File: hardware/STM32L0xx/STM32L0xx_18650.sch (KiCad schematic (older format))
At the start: 50 parts, among them J1 Debug, J2 Battery, J3 GPIO, J4 USB_B_Micro, J5 Power, J6 LEDs, J7 GPIO, Q1 BSS806N, Q2 BSS806N, Q3 BSS806N, Q4 BSS806N, SW1 Mode, SW2 Power, U1 STM32L072CBTx, U2 AP2210N-3.3TRG1, U3 MCP73831T-2ACI/OT, Y1 32.768kHz

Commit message: Add a full 10-pin JTAG connector.
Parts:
- added J8, J9: Conn_01x01, Connector_PinHeader_2.54mm:PinHeader_1x01_P2.54mm_Vertical, symbol Connector_Generic:Conn_01x01
- J1: value Debug -> SW Debug; footprint Connector_PinHeader_1.27mm:PinHeader_1x03_P1.27mm_Vertical -> Connector_PinHeader_1.27mm:PinHeader_2x05_P1.27mm_Vertical; symbol Connector_Generic:Conn_01x03 -> Connector:Conn_ARM_JTAG_SWD_10
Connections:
- wire segments 202 -> 209
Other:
- note added: "JTAG / SWD"
- moved on the sheet: U2
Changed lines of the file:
@@
-$EndComp
-$Comp
-L power:+3V3 #PWR0102
-U 1 1 5BD53A46
-P 5050 6900
-F 0 "#PWR0102" H 5050 6750 50  0001 C CNN
-F 1 "+3V3" H 5065 7073 50  0000 C CNN
-F 2 "" H 5050 6900 50  0001 C CNN
-F 3 "" H 5050 6900 50  0001 C CNN
-	1    5050 6900
-	1    0    0    -1
 $EndComp
 $Comp
@@
 Connection ~ 2700 7400
 NoConn ~ 3050 7100
-$Comp
-L power:GND #PWR0108
-U 1 1 5BD85B6B
-P 4500 7450
-F 0 "#PWR0108" H 4500 7200 50  0001 C CNN
-F 1 "GND" H 4505 7277 50  0000 C CNN
-F 2 "" H 4500 7450 50  0001 C CNN
-F 3 "" H 4500 7450 50  0001 C CNN
-	1    4500 7450
-	1    0    0    -1
-$EndComp
 Text Label 1700 1450 0    50   ~ 0
 VIN
 Wire Wire Line
 	1500 1450 1700 1450
-Text Label 4100 7000 2    50   ~ 0
-VIN
 $Comp
 L STM32L0xx_18650-rescue:MCP73831T-2ACI_OT-LEDRibbonController-rescue-LitFist18650-rescue U?
@@
 Text Notes 2450 6450 0    50   ~ 0
 USB Connector
-Wire Wire Line
-	5050 6900 5050 7000
-Wire Wire Line
-	5050 7000 4950 7000
-Text Notes 3950 6650 0    50   ~ 0
-3.3v Power
 $Comp
 L Transistor_FET:MMBF170 Q?
@@
 Wire Wire Line
 	10100 5400 10400 5400
-$Comp
-L Jeremy:AP2210-3.3TRG1 U2
-U 1 1 5CD3E552
-P 4250 7050
-F 0 "U2" H 4350 6750 50  0000 C CNN
-F 1 "AP2210N-3.3TRG1" H 4525 7234 50  0000 C CNN
-F 2 "Package_TO_SOT_SMD:SOT-23" H 4200 7450 50  0001 C CNN
-F 3 "" H 4200 7450 50  0001 C CNN
-F 4 "AP2210N-3.3TRG1" H 4250 7050 50  0001 C CNN "MPN"
-	1    4250 7050
-	1    0    0    -1
-$EndComp
-Wire Notes Line
-	3950 6650 5200 6650
-Wire Notes Line
-	5200 6650 5200 7700
-Wire Notes Line
-	3950 7700 5200 7700
-Wire Notes Line
-	3950 6650 3950 7700
 Wire Wire Line
 	4450 2800 4300 2800
@@
 Wire Notes Line
 	2450 6450 3700 6450
-Text Label 1850 6100 0    50   ~ 0
-SWDIO
-Text Label 1850 6000 0    50   ~ 0
-SWCLK
-Text Label 1850 5900 0    50   ~ 0
-RESET
 $Comp
 L Device:R R?
@@
 	0    1    1    0
 $EndComp
-$Comp
-L Connector_Generic:Conn_01x03 J1
+Text Label 4800 6800 0    50   ~ 0
+SWDIO
+Text Label 4800 6700 0    50   ~ 0
+SWCLK
+Text Label 4800 6500 0    50   ~ 0
+RESET
+$Comp
+L power:+3.3V #PWR0104
+U 1 1 5D7E89AF
+P 4300 6200
+F 0 "#PWR0104" H 4300 6050 50  0001 C CNN
+F 1 "+3.3V" H 4315 6373 50  0000 C CNN
+F 2 "" H 4300 6200 50  0001 C CNN
+F 3 "" H 4300 6200 50  0001 C CNN
+	1    4300 6200
+	1    0    0    -1
+$EndComp
+$Comp
+L power:GND #PWR0105
+U 1 1 5D7E99F4
+P 4250 7450
+F 0 "#PWR0105" H 4250 7200 50  0001 C CNN
+F 1 "GND" H 4255 7277 50  0000 C CNN
+F 2 "" H 4250 7450 50  0001 C CNN
+F 3 "" H 4250 7450 50  0001 C CNN
+	1    4250 7450
+	1    0    0    -1
+$EndComp
+Wire Wire Line
+	4200 7400 4200 7450
+Wire Wire Line
+	4200 7450 4250 7450
+Wire Wire Line
+	4250 7450 4300 7450
+Wire Wire Line
+	4300 7450 4300 7400
+Connection ~ 4250 7450
+Wire Wire Line
+	4800 6900 4800 7000
+Wire Wire Line
+	4800 7450 4300 7450
+Connection ~ 4800 7000
+Wire Wire Line
+	4800 7000 4800 7450
+Connection ~ 4300 7450
+Wire Notes Line
+	3850 5950 3850 7700
+Wire Notes Line
+	5100 7700 5100 5950
+Wire Notes Line
+	3850 7700 5100 7700
+Wire Notes Line
+	3850 5950 5100 5950
+Wire Notes Line
+	5200 6650 5200 7700
+Wire Notes Line
+	5200 7700 6450 7700
+Wire Notes Line
+	6450 6650 6450 7700
+Wire Notes Line
+	5200 6650 6450 6650
+$Comp
+L Jeremy:AP2210-3.3TRG1 U2
+U 1 1 5CD3E552
+P 5500 7050
+F 0 "U2" H 5600 6750 50  0000 C CNN
+F 1 "AP2210N-3.3TRG1" H 5775 7234 50  0000 C CNN
+F 2 "Package_TO_SOT_SMD:SOT-23" H 5450 7450 50  0001 C CNN
+F 3 "" H 5450 7450 50  0001 C CNN
+F 4 "AP2210N-3.3TRG1" H 5500 7050 50  0001 C CNN "MPN"
+	1    5500 7050
+	1    0    0    -1
+$EndComp
+Text Notes 5200 6650 0    50   ~ 0
+3.3v Power
+Wire Wire Line
+	6300 7000 6200 7000
+Wire Wire Line
+	6300 6900 6300 7000
+Text Label 5350 7000 2    50   ~ 0
+VIN
+$Comp
+L power:GND #PWR0108
+U 1 1 5BD85B6B
+P 5750 7450
+F 0 "#PWR0108" H 5750 7200 50  0001 C CNN
+F 1 "GND" H 5755 7277 50  0000 C CNN
+F 2 "" H 5750 7450 50  0001 C CNN
+F 3 "" H 5750 7450 50  0001 C CNN
+	1    5750 7450
+	1    0    0    -1
+$EndComp
+$Comp
+L power:+3V3 #PWR0102
+U 1 1 5BD53A46
+P 6300 6900
+F 0 "#PWR0102" H 6300 6750 50  0001 C CNN
+F 1 "+3V3" H 6315 7073 50  0000 C CNN
+F 2 "" H 6300 6900 50  0001 C CNN
+F 3 "" H 6300 6900 50  0001 C CNN
+	1    6300 6900
+	1    0    0    -1
+$EndComp
+$Comp
+L Connector:Conn_ARM_JTAG_SWD_10 J1
 U 1 1 5D4460E4
-P 1650 6000
-F 0 "J1" H 1800 6000 50  0000 C CNN
-F 1 "Debug" H 1850 5900 50  0000 C CNN
-F 2 "Connector_PinHeader_1.27mm:PinHeader_1x03_P1.27mm_Vertical" H 1650 6000 50  0001 C CNN
-F 3 "~" H 1650 6000 50  0001 C CNN
-	1    1650 6000
-	-1   0    0    1
+P 4300 6800
+F 0 "J1" H 3950 6200 50  0000 C CNN
+F 1 "SW Debug" H 4550 6250 50  0000 C CNN
+F 2 "Connector_PinHeader_1.27mm:PinHeader_2x05_P1.27mm_Vertical" H 4300 6800 50  0001 C CNN
+F 3 "~" H 4300 6800 50  0001 C CNN
+	1    4300 6800
+	1    0    0    -1
+$EndComp
+Text Notes 3850 5950 0    50   ~ 0
+JTAG / SWD
+Connection ~ 800  6950
+Connection ~ 1200 6950
+$Comp
+L Connector_Generic:Conn_01x01 J8
+U 1 1 5D90FB9A
+P 800 7150
+F 0 "J8" V 900 7100 50  0000 L CNN
+F 1 "Conn_01x01" V 900 7050 50  0001 L CNN
+F 2 "Connector_PinHeader_2.54mm:PinHeader_1x01_P2.54mm_Vertical" H 800 7150 50  0001 C CNN
+F 3 "~" H 800 7150 50  0001 C CNN
+	1    800  7150
+	0    1    1    0
+$EndComp
+$Comp
+L Connector_Generic:Conn_01x01 J9
+U 1 1 5D9108FC
+P 1200 7150
+F 0 "J9" V 1300 7100 50  0000 L CNN
+F 1 "Conn_01x01" V 1300 7050 50  0001 L CNN
+F 2 "Connector_PinHeader_2.54mm:PinHeader_1x01_P2.54mm_Vertical" H 1200 7150 50  0001 C CNN
+F 3 "~" H 1200 7150 50  0001 C CNN
+	1    1200 7150
+	0    1    1    0
 $EndComp
 $EndSCHEMATC

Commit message: Change to 32 pin package.
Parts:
- removed C6: 100nf, Capacitor_SMD:C_0603_1608Metric, symbol Device:C_Small
- D1, D2: footprint Diode_SMD:D_SOD-323 -> Diode_SMD:D_SOD-323_HandSoldering
- U1: value STM32L072CBTx -> STM32L072KZTx; footprint Package_QFP:LQFP-48_7x7mm_P0.5mm -> Package_QFP:LQFP-32_7x7mm_P0.8mm; symbol MCU_ST_STM32L0:STM32L072CBTx -> MCU_ST_STM32L0:STM32L072KZTx; MPN STM32L072CBT6 -> STM32L072KZT6; Package 48-LQFP -> 32-LQFP
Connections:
- net +3V3: now also U1.17 (VDD); no longer U1.24 (VDD), U1.36 (VDD_USB), U1.48 (VDD)
- net BUTTON: now also U1.27 (PB4), U1.31 (BOOT0); no longer U1.40 (PB4), U1.44 (BOOT0)
- net GND: now also U1.16 (VSS), U1.32 (VSS); no longer U1.23 (VSS), U1.35 (VSS), U1.47 (VSS), U1.8 (VSSA)
- net LED1: now also U1.6 (PA0); no longer U1.10 (PA0)
- net LED2: now also U1.7 (PA1); no longer U1.11 (PA1)
- net LED3: now also U1.8 (PA2); no longer U1.12 (PA2)
- net LED4: now also U1.9 (PA3); no longer U1.13 (PA3)
- net PA10: now also U1.20 (PA10); no longer U1.31 (PA10)
- net PA4: now also U1.10 (PA4); no longer U1.14 (PA4)
- net PA5: now also U1.11 (PA5); no longer U1.15 (PA5)
- net PA6: now also U1.12 (PA6); no longer U1.16 (PA6)
- net PA7: now also U1.13 (PA7); no longer U1.17 (PA7)
- net PA8: now also U1.18 (PA8); no longer U1.29 (PA8)
- net PA9: now also U1.19 (PA9); no longer U1.30 (PA9)
- net PB6: now also J7.4 (Pin_4), U1.29 (PB6); no longer J7.3 (Pin_3), U1.42 (PB6)
- net PB7: now also J7.5 (Pin_5), U1.30 (PB7); no longer J7.4 (Pin_4), U1.43 (PB7)
- net RESET: now also U1.4 (NRST); no longer U1.7 (NRST)
- net SWCLK: now also U1.24 (PA14); no longer U1.37 (PA14)
- net SWDIO: now also U1.23 (PA13); no longer U1.34 (PA13)
- net USB_D+: now also U1.22 (PA12); no longer U1.33 (PA12)
- net USB_D-: now also U1.21 (PA11); no longer U1.32 (PA11)
- net at C2.1, C3.1, L1.1: now also U1.5 (VDDA); no longer U1.9 (VDDA)
- net at U1.2 (PC14): now also C8.1, Y1.1
- net PB5: now reaches U1.28 (PB5)
- net PB5: now also J7.3 (Pin_3)
- net at C10.1, Y1.2: now also U1.3 (PC15); no longer U1.4 (PC15)
- removed net PB8: J7.5 (Pin_5), U1.45 (PB8)
- no-connect marks 17 -> 5
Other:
- moved on the sheet: C10, C2, C3, C4, C5, C7, C8, L1, Y1

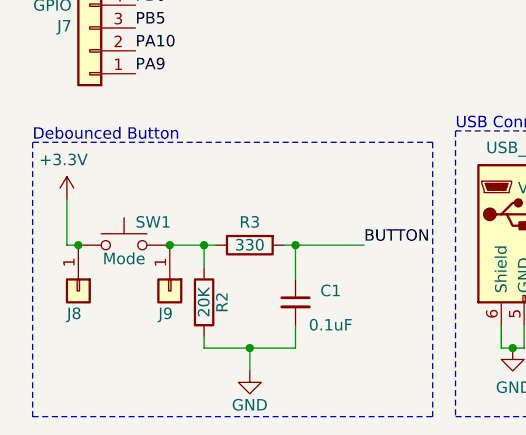
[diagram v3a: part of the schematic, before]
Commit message: Add top labels and cleanup.
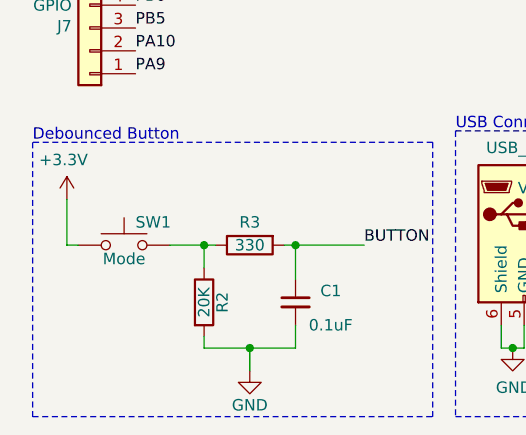
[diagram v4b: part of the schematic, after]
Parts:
- removed J8, J9: Conn_01x01, Connector_PinHeader_2.54mm:PinHeader_1x01_P2.54mm_Vertical, symbol Connector_Generic:Conn_01x01
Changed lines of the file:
@@
 Text Notes 3850 5950 0    50   ~ 0
 JTAG / SWD
-Connection ~ 800  6950
-Connection ~ 1200 6950
-$Comp
-L Connector_Generic:Conn_01x01 J8
-U 1 1 5D90FB9A
-P 800 7150
-F 0 "J8" V 900 7100 50  0000 L CNN
-F 1 "Conn_01x01" V 900 7050 50  0001 L CNN
-F 2 "Connector_PinHeader_2.54mm:PinHeader_1x01_P2.54mm_Vertical" H 800 7150 50  0001 C CNN
-F 3 "~" H 800 7150 50  0001 C CNN
-	1    800  7150
-	0    1    1    0
-$EndComp
-$Comp
-L Connector_Generic:Conn_01x01 J9
-U 1 1 5D9108FC
-P 1200 7150
-F 0 "J9" V 1300 7100 50  0000 L CNN
-F 1 "Conn_01x01" V 1300 7050 50  0001 L CNN
-F 2 "Connector_PinHeader_2.54mm:PinHeader_1x01_P2.54mm_Vertical" H 1200 7150 50  0001 C CNN
-F 3 "~" H 1200 7150 50  0001 C CNN
-	1    1200 7150
-	0    1    1    0
-$EndComp
 Wire Wire Line
 	2800 3450 2850 3450

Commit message: Cleanup.
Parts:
- Q1, Q2, Q3, Q4: Package (none) -> SOT-23
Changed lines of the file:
@@
 F 3 "" H 7150 2500 50  0001 L CNN
 F 4 "BSS806NH6327XTSA1" H 7150 2500 50  0001 C CNN "MPN"
+F 5 "SOT-23" H 7150 2500 50  0001 C CNN "Package"
 	1    7150 2500
 	1    0    0    -1
@@
 F 3 "" H 8050 2500 50  0001 L CNN
 F 4 "BSS806NH6327XTSA1" H 8050 2500 50  0001 C CNN "MPN"
+F 5 "SOT-23" H 8050 2500 50  0001 C CNN "Package"
 	1    8050 2500
 	1    0    0    -1
@@
 F 3 "" H 8900 2500 50  0001 L CNN
 F 4 "BSS806NH6327XTSA1" H 8900 2500 50  0001 C CNN "MPN"
+F 5 "SOT-23" H 8900 2500 50  0001 C CNN "Package"
 	1    8900 2500
 	1    0    0    -1
@@
 F 3 "" H 9750 2500 50  0001 L CNN
 F 4 "BSS806NH6327XTSA1" H 9750 2500 50  0001 C CNN "MPN"
+F 5 "SOT-23" H 9750 2500 50  0001 C CNN "Package"
 	1    9750 2500
 	1    0    0    -1

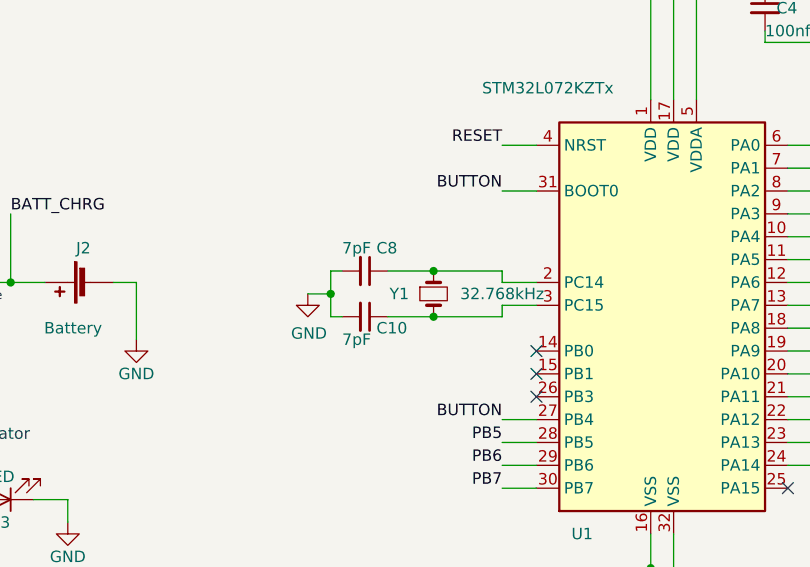
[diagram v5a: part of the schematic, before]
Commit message: Use standard parts/symbols
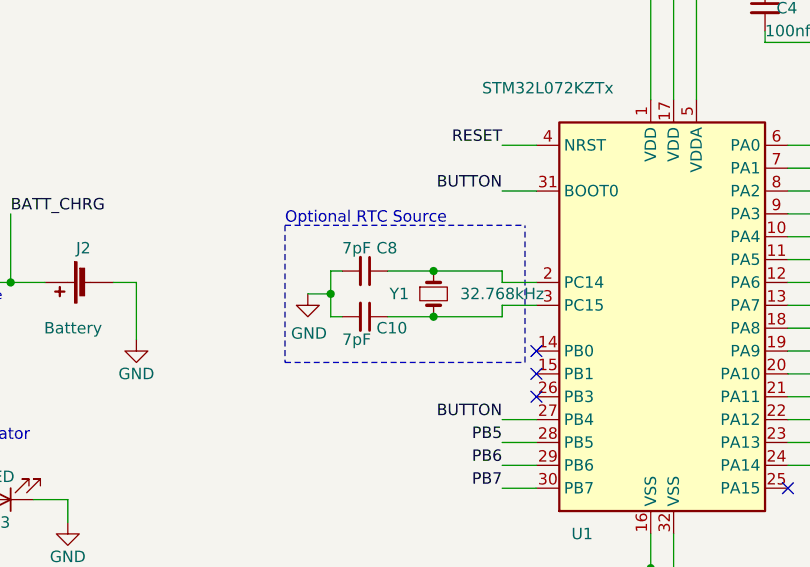
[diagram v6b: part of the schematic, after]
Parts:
- SW1: footprint Jeremy:Switch_TE_FSMSM -> Button_Switch_SMD:SW_SPST_FSMSM
- SW2: footprint Jeremy:Switch_SPST_GPTS203211BR2 -> Button_Switch_THT:SW_CW_GPTS203211B
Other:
- note added: "Optional RTC Source"
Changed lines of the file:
@@
 F 0 "SW2" H 1300 1575 50  0000 C CNN
 F 1 "Power" H 1300 1350 50  0000 C CNN
-F 2 "Jeremy:Switch_SPST_GPTS203211BR2" H 1300 1450 50  0001 C CNN
+F 2 "Button_Switch_THT:SW_CW_GPTS203211B" H 1300 1450 50  0001 C CNN
 F 3 "" H 1300 1450 50  0001 C CNN
 F 4 "GPTS203211B" H 1300 1450 60  0001 C CNN "MPN"
@@
 F 0 "SW1" H 1050 7050 50  0000 L CNN
 F 1 "Mode" H 1000 6890 50  0000 C CNN
-F 2 "Jeremy:Switch_TE_FSMSM" H 1000 7150 50  0001 C CNN
+F 2 "Button_Switch_SMD:SW_SPST_FSMSM" H 1000 7150 50  0001 C CNN
 F 3 "" H 1000 7150 50  0001 C CNN
 F 4 "1437566-3" H 1000 6950 60  0001 C CNN "MPN"
@@
 NoConn ~ 3700 3800
 NoConn ~ 4800 4200
+Wire Notes Line
+	2600 3050 2600 3650
+Wire Notes Line
+	2600 3650 3650 3650
+Wire Notes Line
+	3650 3650 3650 3050
+Wire Notes Line
+	2600 3050 3650 3050
+Text Notes 2600 3050 0    50   ~ 0
+Optional RTC Source
 $EndSCHEMATC

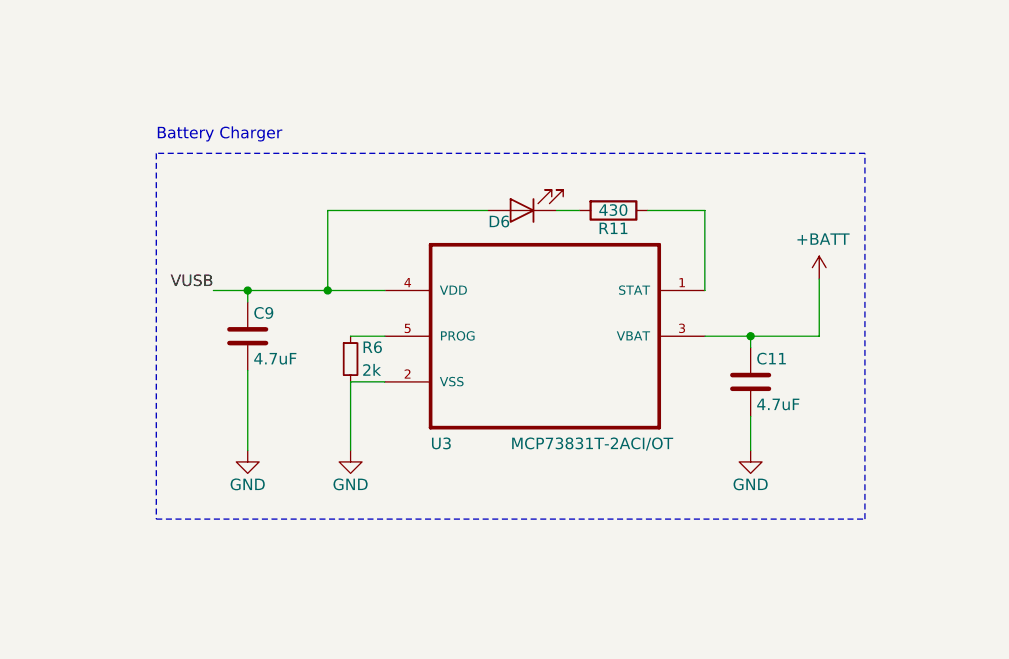
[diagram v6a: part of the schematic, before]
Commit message: Update charger IC (MCP73833-AMI_UN)
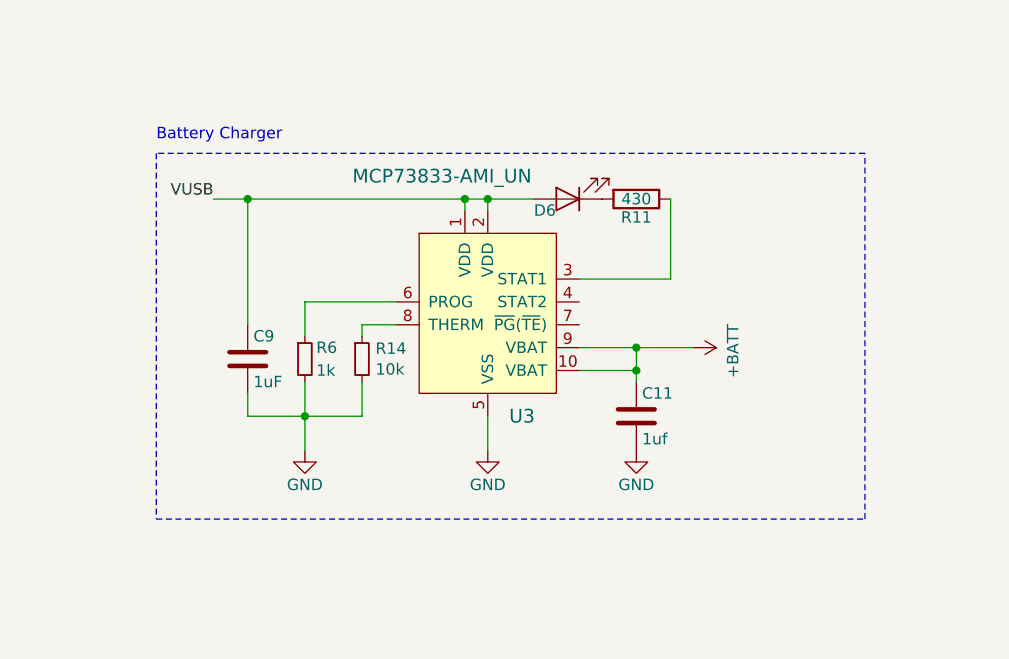
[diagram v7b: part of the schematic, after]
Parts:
- removed U3: MCP73831T-2ACI/OT, Package_TO_SOT_SMD:SOT-23-5_HandSoldering, symbol STM32L0xx_18650-rescue:MCP73831T-2ACI_OT-LEDRibbonController-rescue-LitFist1865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
- added R14: 10k, Resistor_SMD:R_0603_1608Metric, symbol Device:R_Small
- added U3: MCP73833-AMI_UN, Package_SO:TSSOP-10_3x3mm_P0.5mm, symbol dk_PMIC-Battery-Chargers:MCP73833-AMI_UN
- C11: value 4.7uF -> 1uf; MPN KEMET C0603C475K9PACTU -> (none)
- C9: value 4.7uF -> 1uF; MPN KEMET C0603C475K9PACTU -> (none)
- R6: value 2k -> 1k
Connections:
- net +BATT: now also U3.10 (VBAT), U3.9 (VBAT)
- net GND: now also R14.2, U3.5 (VSS)
- net VUSB: now also U3.1 (VDD), U3.2 (VDD)
- net at R11.1: now also U3.3 (STAT1)
- net at R6.1: now also U3.6 (PROG)
- new net: R14.1, U3.8 (THERM)
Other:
- moved on the sheet: C11, C9, D6, R11, R6

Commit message: Convert PCB from 4 layer to 2 layer.
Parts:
- C9: footprint Capacitor_SMD:C_0603_1608Metric_Pad1.05x0.95mm_HandSolder -> Capacitor_SMD:C_0603_1608Metric
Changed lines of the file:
@@
 F 0 "C9" H 7925 5600 50  0000 L CNN
 F 1 "1uF" H 7925 5400 50  0000 L CNN
-F 2 "Capacitor_SMD:C_0603_1608Metric_Pad1.05x0.95mm_HandSolder" H 7938 5350 50  0001 C CNN
+F 2 "Capacitor_SMD:C_0603_1608Metric" H 7938 5350 50  0001 C CNN
 F 3 "" H 7900 5500 50  0001 C CNN
 F 4 "0603" H 0   100 50  0001 C CNN "Package"
